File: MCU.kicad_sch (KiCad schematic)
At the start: 30 parts, among them U4 STM32H723VGTx, Y1 8MHz

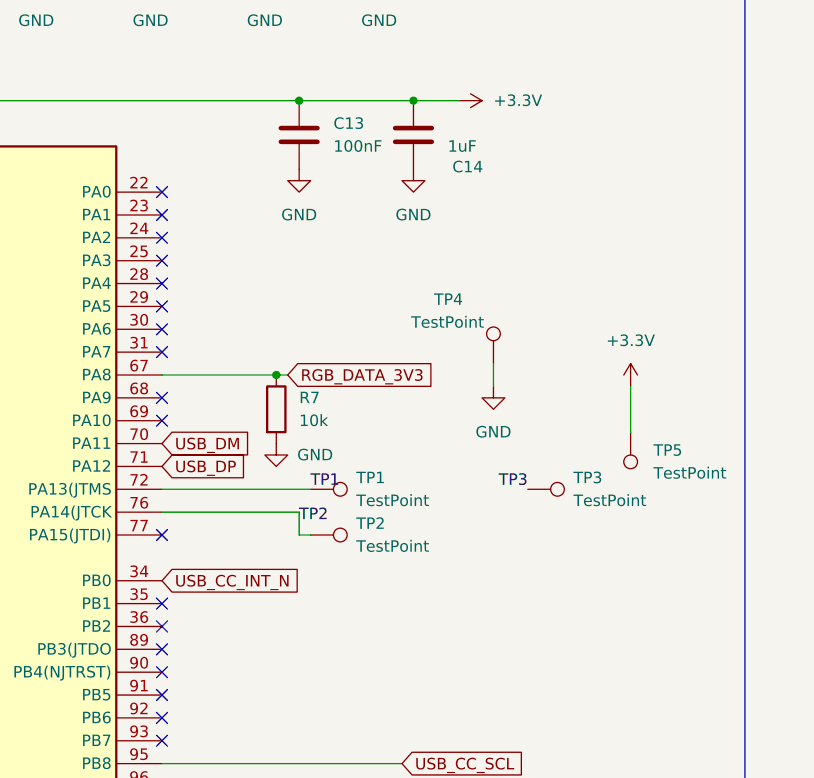
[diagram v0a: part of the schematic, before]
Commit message: Fixed usb routing
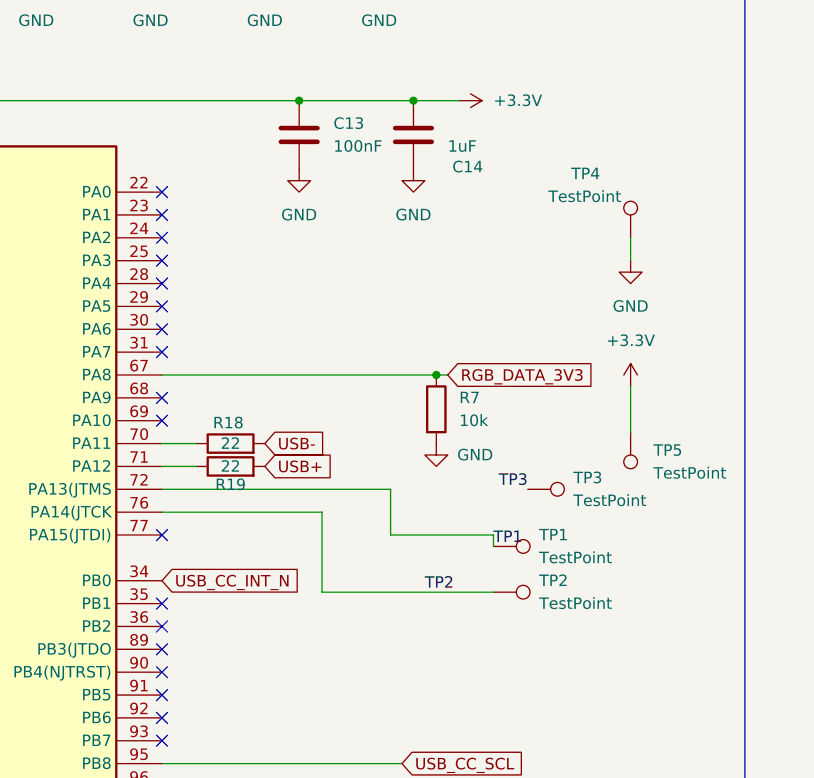
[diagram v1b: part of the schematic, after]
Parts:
- added R18, R19: 22, Resistor_SMD:R_0603_1608Metric, symbol Device:R
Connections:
- net USB_DM: no longer names the net of U4.70 (PA11)
- net USB_DM: now also R18.1
- net USB_DP: no longer names the net of U4.71 (PA12)
- net USB_DP: now also R19.1
- new net USB+: R19.2
- new net USB-: R18.2
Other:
- moved on the sheet: R7, TP1, TP2, TP4
